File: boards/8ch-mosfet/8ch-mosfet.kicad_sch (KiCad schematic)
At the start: 20 parts, among them J1 N2K, J2 I2C, J3 Screw_Terminal_01x09, J4 Screw_Terminal_01x09, M1 Fan_4pin, U1 ESP32-DEVKITC, U2 MCP3208, U3 R-78B3.3-2.0

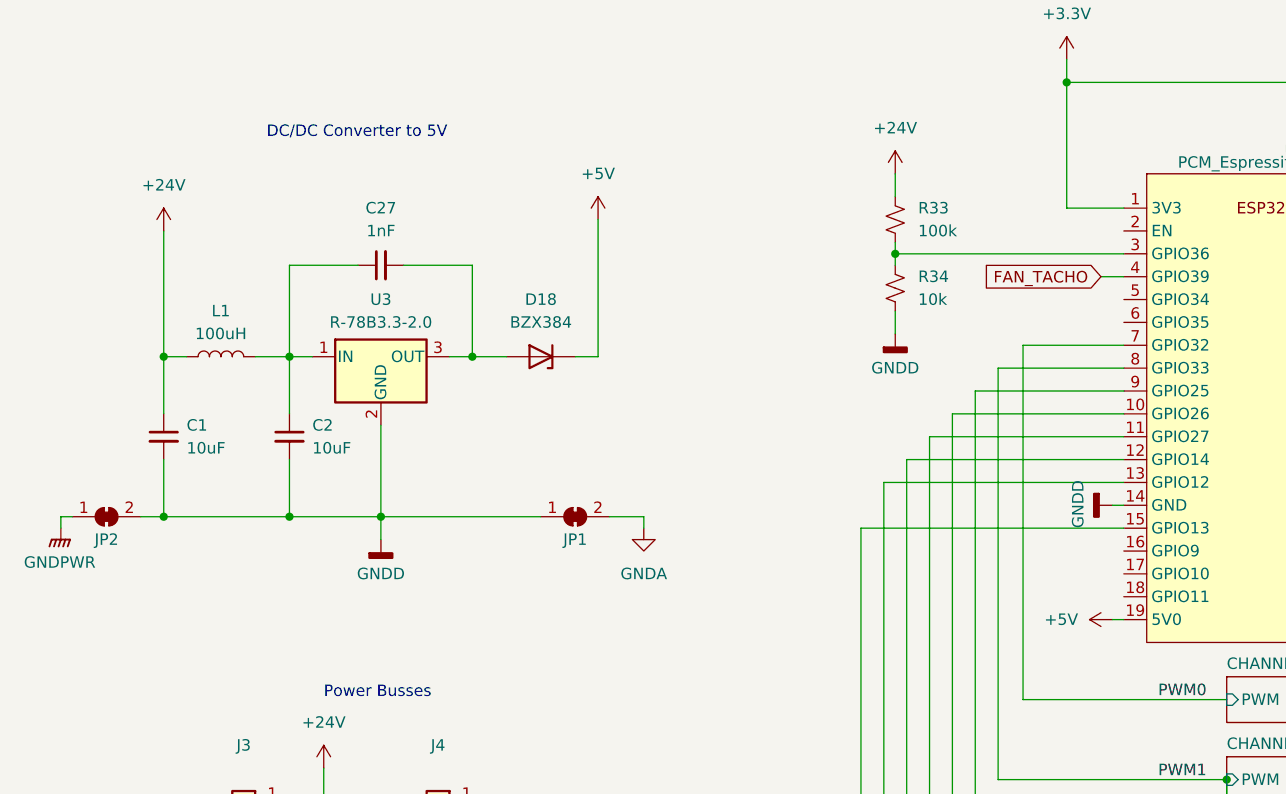
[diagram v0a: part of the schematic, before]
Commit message: changed ground connectors and updated busbar positions.
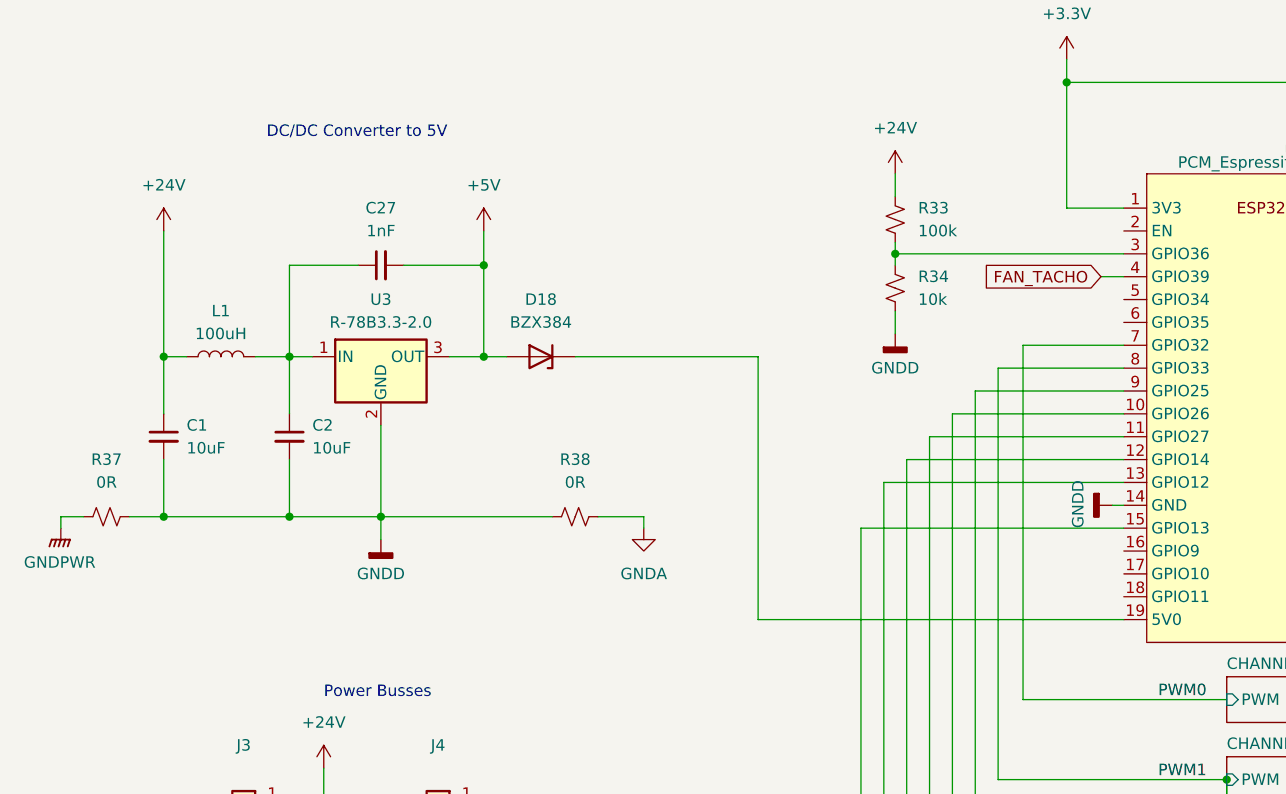
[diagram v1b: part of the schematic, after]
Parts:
- removed JP1, JP2: SolderJumper_2_Bridged, Jumper:SolderJumper-2_P1.3mm_Bridged_RoundedPad1.0x1.5mm, symbol Jumper:SolderJumper_2_Bridged
- added R37, R38: 0R, Resistor_SMD:R_0805_2012Metric_Pad1.20x1.40mm_HandSolder, symbol Device:R_Small_US
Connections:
- net +5V: now also C27.2, D18.2 (A), U3.3 (OUT); no longer D18.1 (K), U1.19 (5V0)
- net GNDA: now also R38.1
- net GNDD: now also R37.1, R38.2
- net GNDPWR: now also R37.2
- new net: D18.1 (K), U1.19 (5V0)

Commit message: updated footprints, changed 5v diode, and added jumpers for fan voltage
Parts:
- removed J3, J4: Screw_Terminal_01x09, gnarboard:Busbar 1x9 .375in, symbol Connector:Screw_Terminal_01x09
- added J3, J4: Screw_Terminal_01x08, gnarboard:Busbar 1x9 .375in, symbol Connector:Screw_Terminal_01x08
- added R39, R40: 0R, Resistor_SMD:R_0805_2012Metric_Pad1.20x1.40mm_HandSolder, symbol Device:R_Small_US
- D18: value BZX384 -> CMHSH5-2L; symbol Device:D_Zener -> Device:D_Schottky; Vendor 771-BZX384-C15115 -> 610-CMHSH5-2L
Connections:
- net +24V: now also J3.1 (Pin_1), J3.2 (Pin_2), J3.3 (Pin_3), J3.4 (Pin_4), J3.5 (Pin_5), J3.6 (Pin_6), J3.7 (Pin_7), J3.8 (Pin_8), R39.1; no longer M1.2 (+)
- net +5V: now also R40.1
- net GNDPWR: now also J4.1 (Pin_1), J4.2 (Pin_2), J4.3 (Pin_3), J4.4 (Pin_4), J4.5 (Pin_5), J4.6 (Pin_6), J4.7 (Pin_7), J4.8 (Pin_8)
- new net: M1.2 (+), R39.2, R40.2
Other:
- note added: "Fan Control"
- moved on the sheet: D18

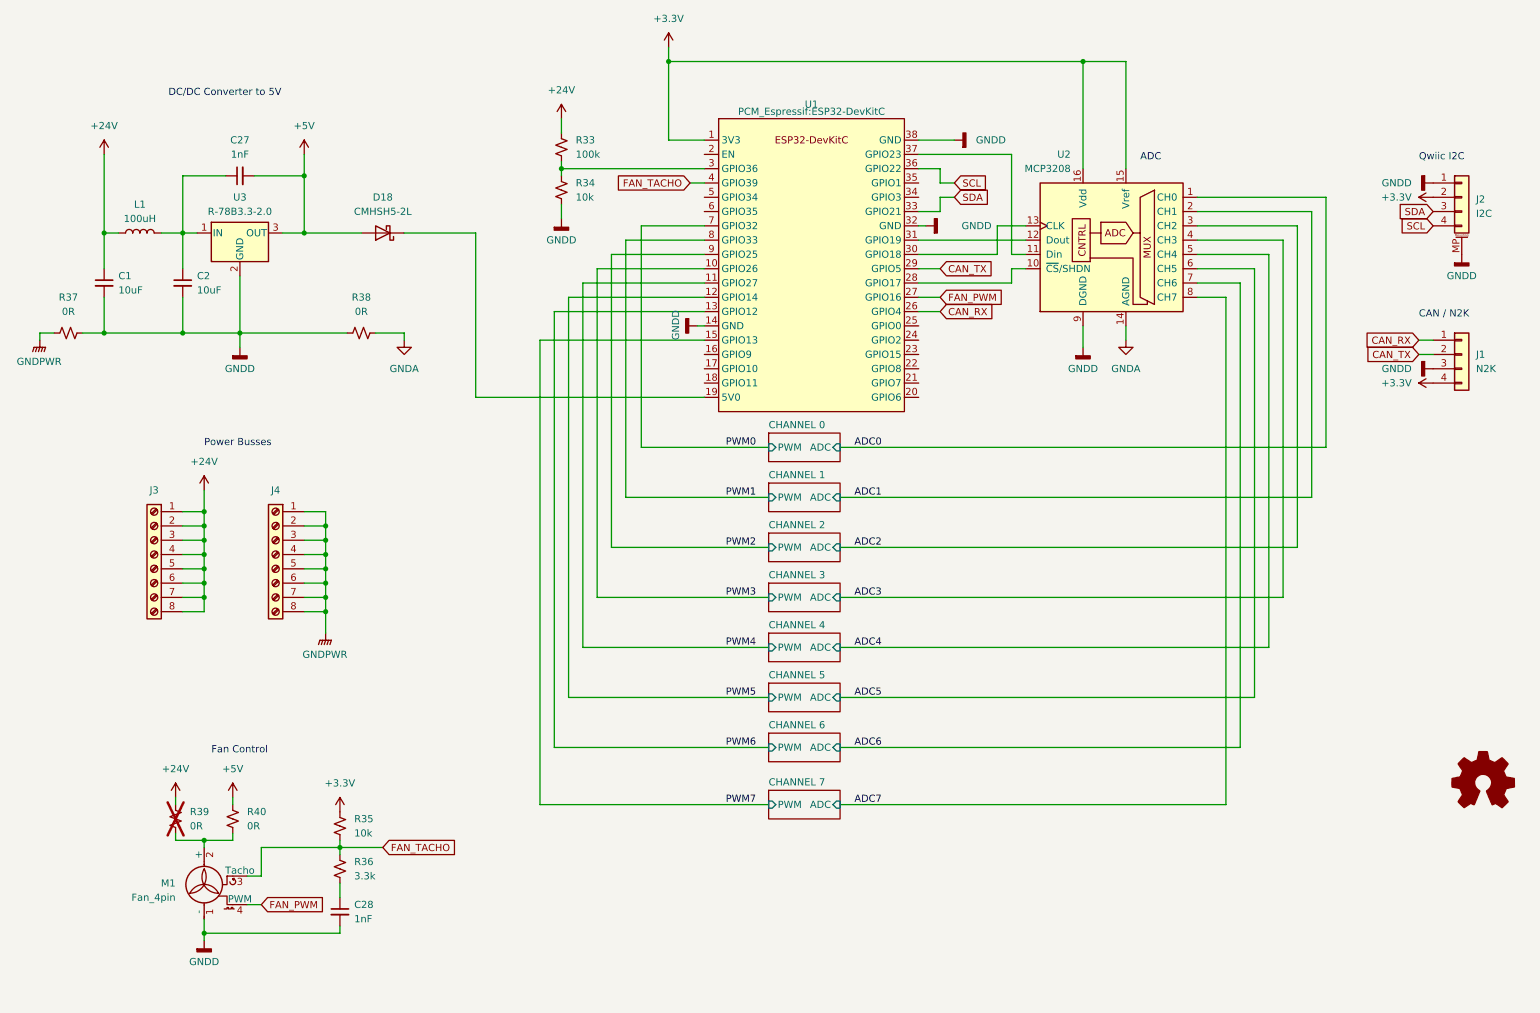
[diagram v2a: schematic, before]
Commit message: added 2nd fan header and simplified circuit.
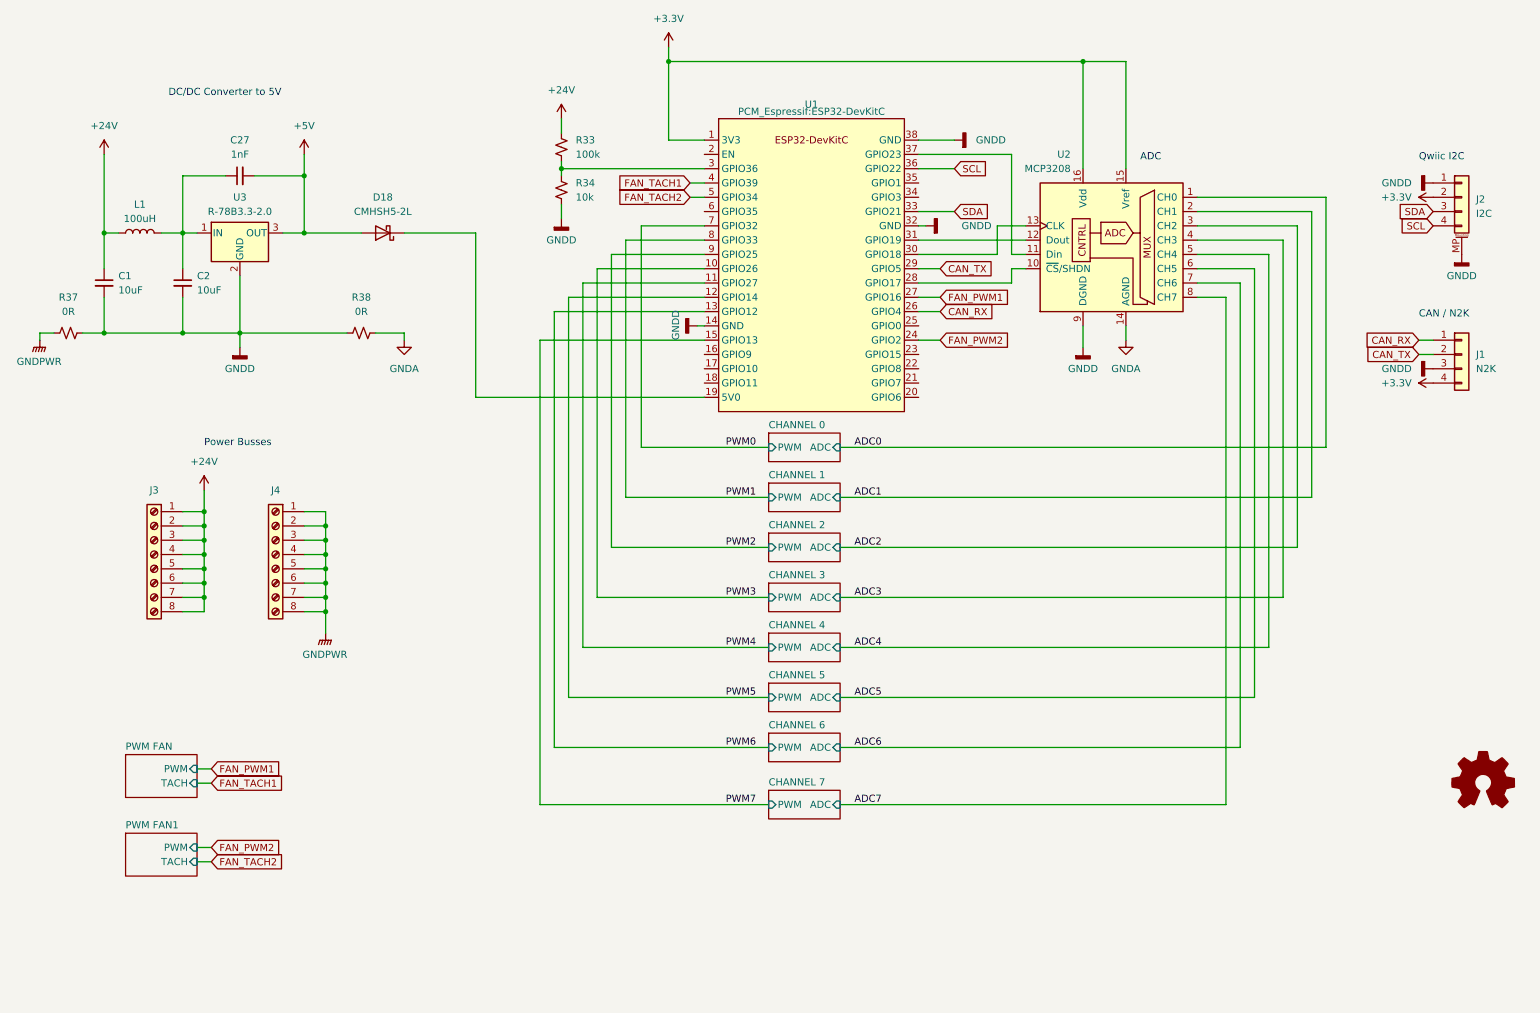
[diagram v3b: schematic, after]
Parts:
- removed C28: 1nF, Capacitor_SMD:C_0805_2012Metric_Pad1.18x1.45mm_HandSolder, symbol Device:C_Small
- removed M1: Fan_4pin, gnarboard:Molex 0470531000, symbol Motor:Fan_4pin
- removed R35: 10k, Resistor_SMD:R_0805_2012Metric_Pad1.20x1.40mm_HandSolder, symbol Device:R_Small_US
- removed R36: 3.3k, Resistor_SMD:R_0805_2012Metric_Pad1.20x1.40mm_HandSolder, symbol Device:R_Small_US
- removed R39, R40: 0R, Resistor_SMD:R_0805_2012Metric_Pad1.20x1.40mm_HandSolder, symbol Device:R_Small_US
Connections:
- net FAN_PWM2: now reaches U1.24 (GPIO2)
- net FAN_TACH2: now reaches U1.5 (GPIO34)
- net FAN_PWM renamed FAN_PWM1
- net FAN_TACHO renamed FAN_TACH1
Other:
- added sheet PWM FAN (pwm fan.kicad_sch)
- added sheet PWM FAN1 (pwm fan.kicad_sch)
- note removed: "Fan Control"
